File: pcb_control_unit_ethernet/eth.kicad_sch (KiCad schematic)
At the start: 31 parts, among them J3 HR911105A, U2 LAN8742A, Y1 25MHz

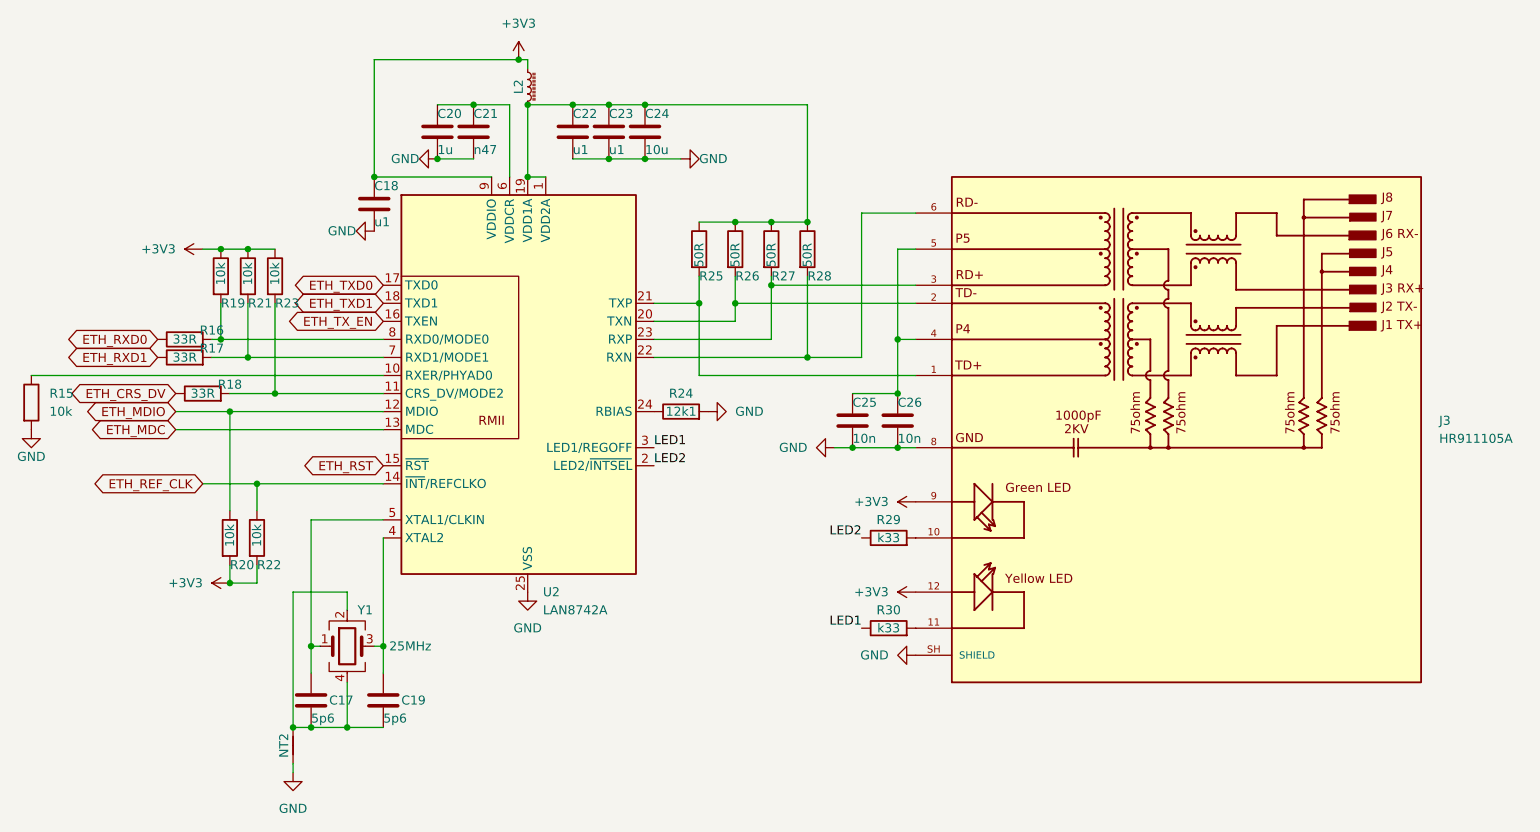
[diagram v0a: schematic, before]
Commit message: First time zero errors, but bad layout
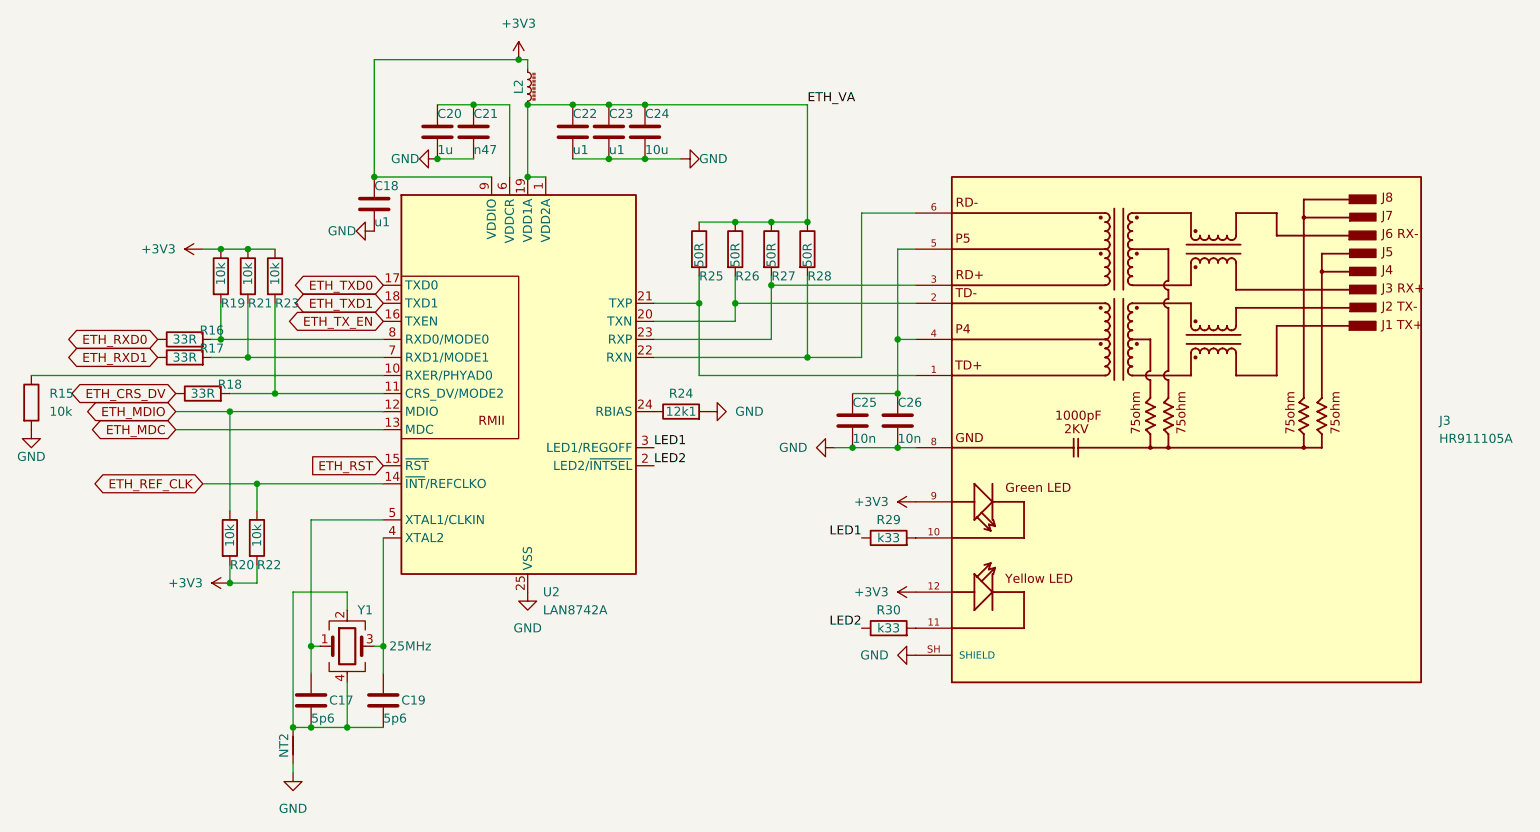
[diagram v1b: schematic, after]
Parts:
- Y1: footprint (none) -> Crystal:Crystal_SMD_2016-4Pin_2.0x1.6mm
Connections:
- net LED1: now also R29.1; no longer R30.1
- net LED2: now also R30.1; no longer R29.1
- net ETH_VA: now reaches C22.1, C23.1, C24.1, L2.2, R25.1, R26.1, R27.1, R28.1, U2.1 (VDD2A), U2.19 (VDD1A)
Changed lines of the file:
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@@
+		)
+	)
+	(label "ETH_VA"
+		(at 144.78 36.83 0)
+		(effects
+			(font
+				(size 1.27 1.27)
+			)
+			(justify left bottom)
 		)
 	)
 	(label "LED2"
-		(at 152.4 97.79 180)
+		(at 152.4 110.49 180)
 		(effects
 			(font
@@
 	)
 	(label "LED1"
-		(at 152.4 110.49 180)
+		(at 152.4 97.79 180)
 		(effects
 			(font
@@
 	)
 	(global_label "ETH_RST"
-		(shape bidirectional)
+		(shape input)
 		(at 85.09 87.63 180)
 		(fields_autoplaced yes)
@@
 		)
 		(property "Intersheetrefs" "${INTERSHEET_REFS}"
-			(at 73.1317 87.63 0)
+			(at 74.243 87.63 0)
 			(effects
 				(font
@@
 			)
 		)
-		(property "Footprint" ""
+		(property "Footprint" "Crystal:Crystal_SMD_2016-4Pin_2.0x1.6mm"
 			(at 80.01 113.03 0)
 			(effects

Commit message: WIP 2nd
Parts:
- removed J3: HR911105A, liebler_CONN:RJ45_HANRUN_HR911105A, symbol liebler_CONN:HR911105A
- added X4: HR911105A_small, liebler_CONN:RJ45_HANRUN_HR911105A, symbol liebler_CONN:HR911105A_small
- R25, R26, R27, R28: value 50R -> 49R9
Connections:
- net +3V3: now also X4.12, X4.9
- net LED1: now also R29.2; no longer R29.1
- net LED2: now also R30.2; no longer R30.1
- net at R26.2, U2.20 (TXN): now also X4.2 (TD-)
- net at R25.2, U2.21 (TXP): now also X4.1 (TD+)
- net at R28.2, U2.22 (RXN): now also X4.6 (RD-)
- net at R27.2, U2.23 (RXP): now also X4.3 (RD+)
- net at C25.1, C26.1: now also X4.4 (TCT), X4.5 (RCT)
- new net: R29.1, X4.10
- new net: R30.1, X4.11
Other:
- moved on the sheet: R29, R30
